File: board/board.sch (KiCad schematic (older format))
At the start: 15 parts, among them J1 MOTION DETECTOR, J2 EXT BUTTON, U3 ATTINY85-20PU

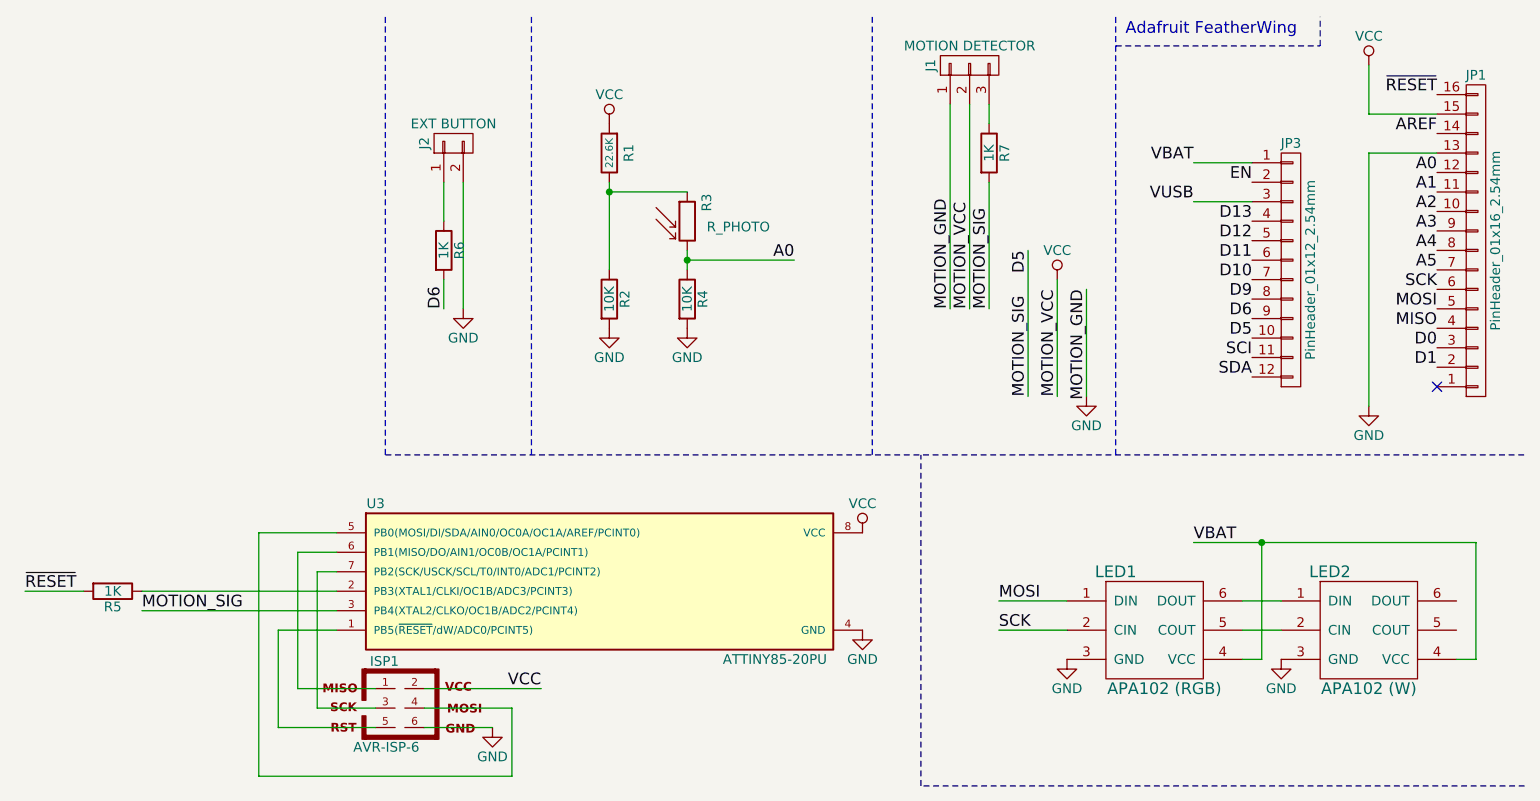
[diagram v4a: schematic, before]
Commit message: Fix photoresistor circuit
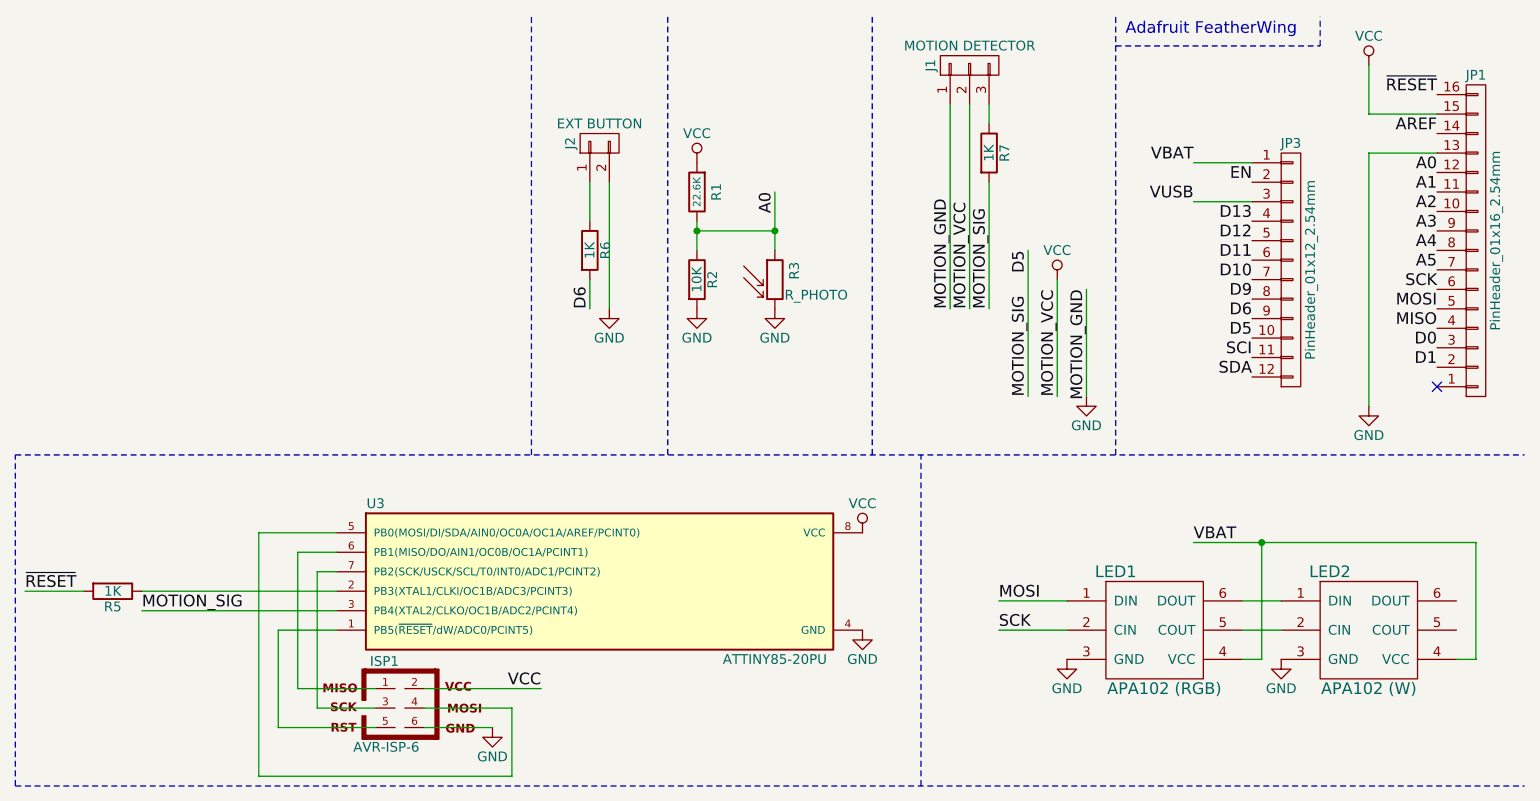
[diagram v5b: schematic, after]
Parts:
- removed R4: 10K, Resistors_SMD:R_0805_HandSoldering, symbol R
- J2: footprint Pin_Headers:Pin_Header_Angled_1x02_Pitch2.54mm -> Pin_Headers:Pin_Header_Straight_1x02_Pitch2.54mm
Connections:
- net A0: now also R1.1, R2.1, R3.1; no longer R3.2
- net GND: now also R3.2
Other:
- moved on the sheet: J2, R1, R2, R3, R6
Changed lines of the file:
@@
 SDA
 Wire Notes Line
-	4650 2750 10500 2750
+	2750 2750 10500 2750
 Wire Notes Line
 	8400 2750 8400 500
@@
 L R_PHOTO R3
 U 1 1 59797B58
-P 6200 1550
-F 0 "R3" V 6300 1600 50  0000 L CNN
-F 1 "R_PHOTO" H 6300 1550 50  0000 L TNN
-F 2 "Opto-Devices:Resistor_LDR_5.1x4.3_RM3.4" V 6250 1300 50  0001 L CNN
-F 3 "" H 6200 1500 50  0001 C CNN
-	1    6200 1550
+P 6650 1850
+F 0 "R3" V 6750 1850 50  0000 L CNN
+F 1 "R_PHOTO" H 6700 1800 50  0000 L TNN
+F 2 "Opto-Devices:Resistor_LDR_5.1x4.3_RM3.4" V 6700 1600 50  0001 L CNN
+F 3 "" H 6650 1800 50  0001 C CNN
+	1    6650 1850
 	1    0    0    -1
 $EndComp
@@
 L R R1
 U 1 1 597CE41F
-P 5800 1200
-F 0 "R1" V 5700 1200 50  0000 C CNN
-F 1 "22.6K" V 5800 1200 39  0000 C CNN
-F 2 "Resistors_SMD:R_0805_HandSoldering" V 5730 1200 50  0001 C CNN
-F 3 "" H 5800 1200 50  0001 C CNN
-	1    5800 1200
+P 6250 1400
+F 0 "R1" V 6150 1400 50  0000 C CNN
+F 1 "22.6K" V 6250 1400 39  0000 C CNN
+F 2 "Resistors_SMD:R_0805_HandSoldering" V 6180 1400 50  0001 C CNN
+F 3 "" H 6250 1400 50  0001 C CNN
+	1    6250 1400
 	-1   0    0    1
 $EndComp
@@
 L R R2
 U 1 1 597CE47C
-P 5800 1950
-F 0 "R2" V 5880 1950 50  0000 C CNN
-F 1 "10K" V 5800 1950 50  0000 C CNN
-F 2 "Resistors_SMD:R_0805_HandSoldering" V 5730 1950 50  0001 C CNN
-F 3 "" H 5800 1950 50  0001 C CNN
-	1    5800 1950
-	1    0    0    -1
-$EndComp
-Wire Wire Line
-	5800 1350 5800 1800
-Wire Wire Line
-	5800 1400 6200 1400
-Connection ~ 5800 1400
+P 6250 1850
+F 0 "R2" V 6330 1850 50  0000 C CNN
+F 1 "10K" V 6250 1850 50  0000 C CNN
+F 2 "Resistors_SMD:R_0805_HandSoldering" V 6180 1850 50  0001 C CNN
+F 3 "" H 6250 1850 50  0001 C CNN
+	1    6250 1850
+	1    0    0    -1
+$EndComp
+Wire Wire Line
+	6250 1550 6250 1700
+Connection ~ 6250 1600
 $Comp
 L GND #PWR04
 U 1 1 597CE63C
-P 5800 2100
-F 0 "#PWR04" H 5800 1850 50  0001 C CNN
-F 1 "GND" H 5800 1950 50  0000 C CNN
-F 2 "" H 5800 2100 50  0001 C CNN
-F 3 "" H 5800 2100 50  0001 C CNN
-	1    5800 2100
+P 6250 2000
+F 0 "#PWR04" H 6250 1750 50  0001 C CNN
+F 1 "GND" H 6250 1850 50  0000 C CNN
+F 2 "" H 6250 2000 50  0001 C CNN
+F 3 "" H 6250 2000 50  0001 C CNN
+	1    6250 2000
 	1    0    0    -1
 $EndComp
@@
 L VCC #PWR05
 U 1 1 597CEF49
-P 5800 1050
-F 0 "#PWR05" H 5800 900 50  0001 C CNN
-F 1 "VCC" H 5800 1200 50  0000 C CNN
-F 2 "" H 5800 1050 50  0001 C CNN
-F 3 "" H 5800 1050 50  0001 C CNN
-	1    5800 1050
-	1    0    0    -1
-$EndComp
-Text Label 6750 1750 2    60   ~ 0
+P 6250 1250
+F 0 "#PWR05" H 6250 1100 50  0001 C CNN
+F 1 "VCC" H 6250 1400 50  0000 C CNN
+F 2 "" H 6250 1250 50  0001 C CNN
+F 3 "" H 6250 1250 50  0001 C CNN
+	1    6250 1250
+	1    0    0    -1
+$EndComp
+Text Label 6650 1400 3    60   ~ 0
 A0
-Wire Wire Line
-	6200 1750 6750 1750
-$Comp
-L R R4
-U 1 1 597D09D1
-P 6200 1950
-F 0 "R4" V 6280 1950 50  0000 C CNN
-F 1 "10K" V 6200 1950 50  0000 C CNN
-F 2 "Resistors_SMD:R_0805_HandSoldering" V 6130 1950 50  0001 C CNN
-F 3 "" H 6200 1950 50  0001 C CNN
-	1    6200 1950
-	1    0    0    -1
-$EndComp
 $Comp
 L GND #PWR06
 U 1 1 597D0A0F
-P 6200 2100
-F 0 "#PWR06" H 6200 1850 50  0001 C CNN
-F 1 "GND" H 6200 1950 50  0000 C CNN
-F 2 "" H 6200 2100 50  0001 C CNN
-F 3 "" H 6200 2100 50  0001 C CNN
-	1    6200 2100
-	1    0    0    -1
-$EndComp
-Wire Wire Line
-	6200 1700 6200 1800
-Connection ~ 6200 1750
+P 6650 2000
+F 0 "#PWR06" H 6650 1750 50  0001 C CNN
+F 1 "GND" H 6650 1850 50  0000 C CNN
+F 2 "" H 6650 2000 50  0001 C CNN
+F 3 "" H 6650 2000 50  0001 C CNN
+	1    6650 2000
+	1    0    0    -1
+$EndComp
+Wire Wire Line
+	6650 1400 6650 1700
+Connection ~ 6650 1600
 $Comp
 L GND #PWR07
@@
 	7150 2750 7150 500
 Wire Notes Line
-	5400 2750 5400 500
-Wire Notes Line
-	10500 4450 7400 4450
+	6100 2750 6100 500
+Wire Notes Line
+	2750 4450 10500 4450
 Wire Notes Line
 	7400 4450 7400 2750
@@
 L CONN_01X02 J2
 U 1 1 597D1FB0
-P 5000 1150
-F 0 "J2" H 5000 1300 50  0000 C CNN
-F 1 "EXT BUTTON" V 5100 1150 50  0000 C CNN
-F 2 "Pin_Headers:Pin_Header_Angled_1x02_Pitch2.54mm" H 5000 1150 50  0001 C CNN
-F 3 "" H 5000 1150 50  0001 C CNN
-	1    5000 1150
+P 5750 1150
+F 0 "J2" H 5750 1300 50  0000 C CNN
+F 1 "EXT BUTTON" V 5850 1150 50  0000 C CNN
+F 2 "Pin_Headers:Pin_Header_Straight_1x02_Pitch2.54mm" H 5750 1150 50  0001 C CNN
+F 3 "" H 5750 1150 50  0001 C CNN
+	1    5750 1150
 	0    -1   -1   0
 $EndComp
@@
 L GND #PWR08
 U 1 1 597D2087
-P 5050 2000
-F 0 "#PWR08" H 5050 1750 50  0001 C CNN
-F 1 "GND" H 5050 1850 50  0000 C CNN
-F 2 "" H 5050 2000 50  0001 C CNN
-F 3 "" H 5050 2000 50  0001 C CNN
-	1    5050 2000
-	1    0    0    -1
-$EndComp
-Wire Wire Line
-	5050 1350 5050 2000
-Wire Wire Line
-	4950 1350 4950 1550
-Text Label 4950 2000 1    60   ~ 0
+P 5800 2000
+F 0 "#PWR08" H 5800 1750 50  0001 C CNN
+F 1 "GND" H 5800 1850 50  0000 C CNN
+F 2 "" H 5800 2000 50  0001 C CNN
+F 3 "" H 5800 2000 50  0001 C CNN
+	1    5800 2000
+	1    0    0    -1
+$EndComp
+Wire Wire Line
+	5800 1350 5800 2000
+Wire Wire Line
+	5700 1350 5700 1550
+Text Label 5700 2000 1    60   ~ 0
 D6
 Wire Notes Line
-	4650 2750 4650 500
+	5400 2750 5400 500
 $Comp
 L ATTINY85-20PU U3
@@
 L R R6
 U 1 1 5982A5C8
-P 4950 1700
-F 0 "R6" V 5030 1700 50  0000 C CNN
-F 1 "1K" V 4950 1700 50  0000 C CNN
-F 2 "Resistors_SMD:R_0805_HandSoldering" V 4880 1700 50  0001 C CNN
-F 3 "" H 4950 1700 50  0001 C CNN
-	1    4950 1700
-	1    0    0    -1
-$EndComp
-Wire Wire Line
-	4950 1850 4950 2000
+P 5700 1700
+F 0 "R6" V 5780 1700 50  0000 C CNN
+F 1 "1K" V 5700 1700 50  0000 C CNN
+F 2 "Resistors_SMD:R_0805_HandSoldering" V 5630 1700 50  0001 C CNN
+F 3 "" H 5700 1700 50  0001 C CNN
+	1    5700 1700
+	1    0    0    -1
+$EndComp
+Wire Wire Line
+	5700 1850 5700 2000
 $Comp
 L R R7
@@
 $EndComp
 $Comp
-L VCC #PWR?
+L VCC #PWR013
 U 1 1 5987EE9E
 P 7100 3150
-F 0 "#PWR?" H 7100 3000 50  0001 C CNN
+F 0 "#PWR013" H 7100 3000 50  0001 C CNN
 F 1 "VCC" H 7100 3300 50  0000 C CNN
 F 2 "" H 7100 3150 50  0001 C CNN
@@
 	1    0    0    -1
 $EndComp
+Wire Wire Line
+	6250 1600 6650 1600
+Wire Notes Line
+	2750 4450 2750 2750
 $EndSCHEMATC

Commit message: Add I2C lines between between attiny and ESP8266
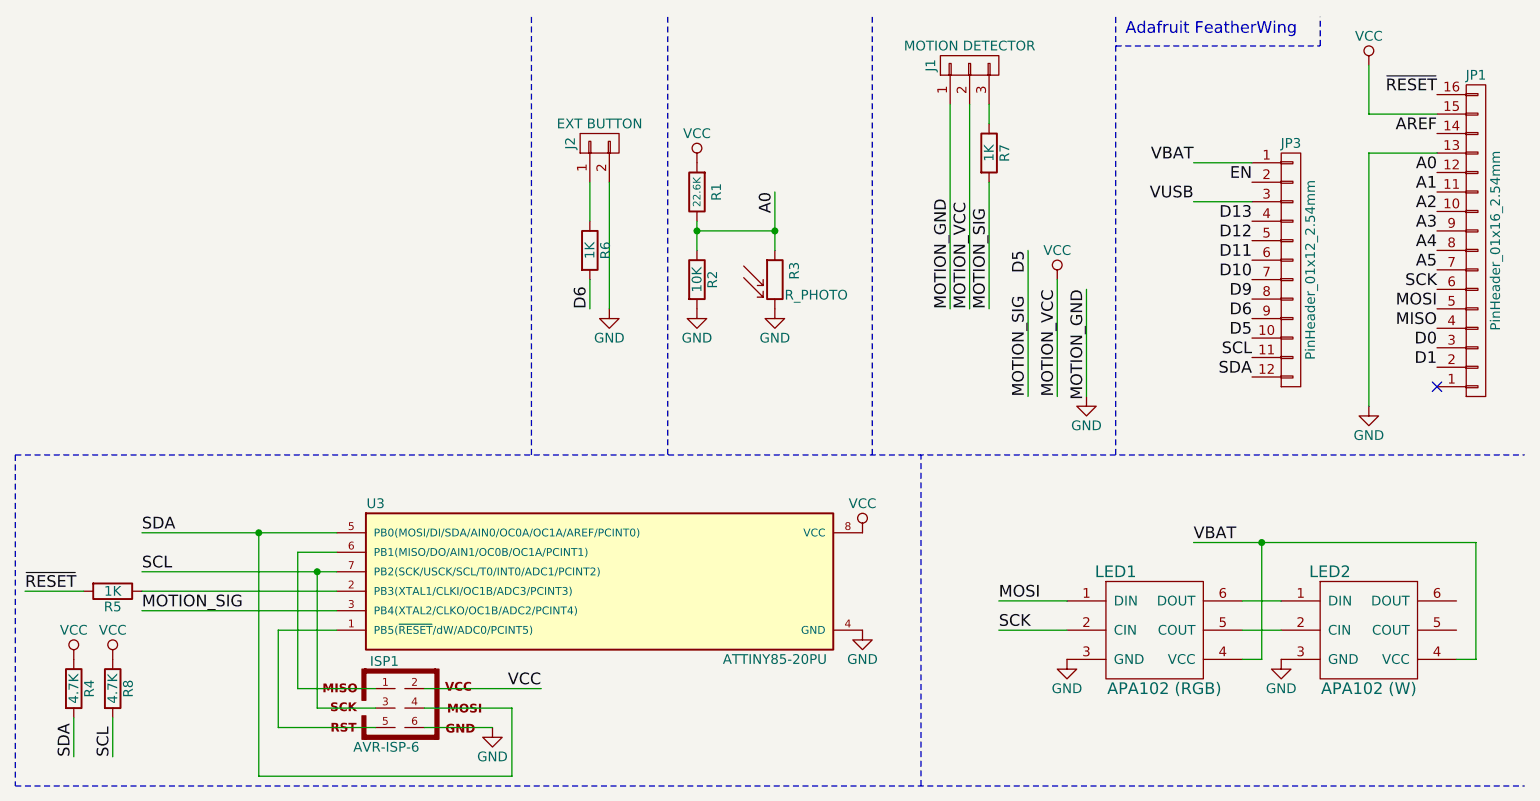
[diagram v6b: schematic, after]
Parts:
- added R4, R8: 4.7K, symbol R
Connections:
- net SCI is gone; now on net SCL: JP3.11 (P11)
- net SDA: now also ISP1.4, U3.5 (PB0(MOSI/DI/SDA/AIN0/OC0A/OC1A/AREF/PCINT0)), R4.2
- net VCC: now also R4.1, R8.1
- net SCL: now reaches ISP1.3, U3.7 (PB2(SCK/USCK/SCL/T0/INT0/ADC1/PCINT2))
- net SCL: now also R8.2
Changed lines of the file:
@@
 Adafruit FeatherWing\n
 $Comp
-L VCC #PWR01
+L VCC #PWR14
 U 1 1 56D753B8
 P 9700 750
-F 0 "#PWR01" H 9700 600 50  0001 C CNN
+F 0 "#PWR14" H 9700 600 50  0001 C CNN
 F 1 "VCC" H 9700 900 50  0000 C CNN
 F 2 "" H 9700 750 50  0000 C CNN
@@
 $EndComp
 $Comp
-L GND #PWR02
+L GND #PWR15
 U 1 1 56D75A03
 P 9700 2500
-F 0 "#PWR02" H 9700 2250 50  0001 C CNN
+F 0 "#PWR15" H 9700 2250 50  0001 C CNN
 F 1 "GND" H 9700 2350 50  0000 C CNN
 F 2 "" H 9700 2500 50  0000 C CNN
@@
 D5
 Text Label 9100 2250 2    60   ~ 0
-SCI
+SCL
 Text Label 9100 2350 2    60   ~ 0
 SDA
@@
 NoConn ~ 10050 2400
 $Comp
-L GND #PWR03
+L GND #PWR11
 U 1 1 59796D2F
 P 8150 3800
-F 0 "#PWR03" H 8150 3550 50  0001 C CNN
+F 0 "#PWR11" H 8150 3550 50  0001 C CNN
 F 1 "GND" H 8150 3650 50  0000 C CNN
 F 2 "" H 8150 3800 50  0001 C CNN
@@
 Connection ~ 6250 1600
 $Comp
-L GND #PWR04
+L GND #PWR6
 U 1 1 597CE63C
 P 6250 2000
-F 0 "#PWR04" H 6250 1750 50  0001 C CNN
+F 0 "#PWR6" H 6250 1750 50  0001 C CNN
 F 1 "GND" H 6250 1850 50  0000 C CNN
 F 2 "" H 6250 2000 50  0001 C CNN
@@
 $EndComp
 $Comp
-L VCC #PWR05
+L VCC #PWR5
 U 1 1 597CEF49
 P 6250 1250
-F 0 "#PWR05" H 6250 1100 50  0001 C CNN
+F 0 "#PWR5" H 6250 1100 50  0001 C CNN
 F 1 "VCC" H 6250 1400 50  0000 C CNN
 F 2 "" H 6250 1250 50  0001 C CNN
@@
 A0
 $Comp
-L GND #PWR06
+L GND #PWR7
 U 1 1 597D0A0F
 P 6650 2000
-F 0 "#PWR06" H 6650 1750 50  0001 C CNN
+F 0 "#PWR7" H 6650 1750 50  0001 C CNN
 F 1 "GND" H 6650 1850 50  0000 C CNN
 F 2 "" H 6650 2000 50  0001 C CNN
@@
 Connection ~ 6650 1600
 $Comp
-L GND #PWR07
+L GND #PWR12
 U 1 1 597D0EF3
 P 8250 2450
-F 0 "#PWR07" H 8250 2200 50  0001 C CNN
+F 0 "#PWR12" H 8250 2200 50  0001 C CNN
 F 1 "GND" H 8250 2300 50  0000 C CNN
 F 2 "" H 8250 2450 50  0001 C CNN
@@
 $EndComp
 $Comp
-L GND #PWR08
+L GND #PWR4
 U 1 1 597D2087
 P 5800 2000
-F 0 "#PWR08" H 5800 1750 50  0001 C CNN
+F 0 "#PWR4" H 5800 1750 50  0001 C CNN
 F 1 "GND" H 5800 1850 50  0000 C CNN
 F 2 "" H 5800 2000 50  0001 C CNN
@@
 $EndComp
 $Comp
-L GND #PWR09
+L GND #PWR9
 U 1 1 597D1088
 P 7100 3650
-F 0 "#PWR09" H 7100 3400 50  0001 C CNN
+F 0 "#PWR9" H 7100 3400 50  0001 C CNN
 F 1 "GND" H 7100 3500 50  0000 C CNN
 F 2 "" H 7100 3650 50  0001 C CNN
@@
 	4300 4050 4300 3350
 Wire Wire Line
-	4300 3350 4400 3350
-$Comp
-L GND #PWR010
+	3400 3350 4400 3350
+$Comp
+L GND #PWR3
 U 1 1 597D12FA
 P 5200 4150
-F 0 "#PWR010" H 5200 3900 50  0001 C CNN
+F 0 "#PWR3" H 5200 3900 50  0001 C CNN
 F 1 "GND" H 5200 4000 50  0000 C CNN
 F 2 "" H 5200 4150 50  0001 C CNN
@@
 	4000 3150 4000 4400
 Wire Wire Line
-	4000 3150 4400 3150
+	3400 3150 4400 3150
 Wire Wire Line
 	4850 4050 5300 4050
@@
 	8100 2450 8100 1850
 $Comp
-L VCC #PWR011
+L VCC #PWR10
 U 1 1 597D3E37
 P 8100 1850
-F 0 "#PWR011" H 8100 1700 50  0001 C CNN
+F 0 "#PWR10" H 8100 1700 50  0001 C CNN
 F 1 "VCC" H 8100 2000 50  0000 C CNN
 F 2 "" H 8100 1850 50  0001 C CNN
@@
 	7750 2000 7750 1350
 $Comp
-L GND #PWR012
+L GND #PWR13
 U 1 1 5986A206
 P 9250 3800
-F 0 "#PWR012" H 9250 3550 50  0001 C CNN
+F 0 "#PWR13" H 9250 3550 50  0001 C CNN
 F 1 "GND" H 9250 3650 50  0000 C CNN
 F 2 "" H 9250 3800 50  0001 C CNN
@@
 $EndComp
 $Comp
-L VCC #PWR013
+L VCC #PWR8
 U 1 1 5987EE9E
 P 7100 3150
-F 0 "#PWR013" H 7100 3000 50  0001 C CNN
+F 0 "#PWR8" H 7100 3000 50  0001 C CNN
 F 1 "VCC" H 7100 3300 50  0000 C CNN
 F 2 "" H 7100 3150 50  0001 C CNN
@@
 Wire Wire Line
 	6250 1600 6650 1600
-Wire Notes Line
-	2750 4450 2750 2750
+Connection ~ 4000 3150
+Connection ~ 4300 3350
+Text Label 3400 3350 0    60   ~ 0
+SCL
+Text Label 3400 3150 0    60   ~ 0
+SDA
+$Comp
+L VCC #PWR2
+U 1 1 598F5087
+P 3250 3800
+F 0 "#PWR2" H 3250 3650 50  0001 C CNN
+F 1 "VCC" H 3250 3950 50  0000 C CNN
+F 2 "" H 3250 3800 50  0001 C CNN
+F 3 "" H 3250 3800 50  0001 C CNN
+	1    3250 3800
+	1    0    0    -1
+$EndComp
+Wire Wire Line
+	3250 4100 3250 4300
+Text Label 3250 4300 1    60   ~ 0
+SCL
+$Comp
+L VCC #PWR1
+U 1 1 598F54B3
+P 3050 3800
+F 0 "#PWR1" H 3050 3650 50  0001 C CNN
+F 1 "VCC" H 3050 3950 50  0000 C CNN
+F 2 "" H 3050 3800 50  0001 C CNN
+F 3 "" H 3050 3800 50  0001 C CNN
+	1    3050 3800
+	1    0    0    -1
+$EndComp
+Wire Wire Line
+	3050 4100 3050 4300
+Text Label 3050 4300 1    60   ~ 0
+SDA
+Wire Notes Line
+	2750 2750 2750 4450
+$Comp
+L R R4
+U 1 1 598F56B4
+P 3050 3950
+F 0 "R4" V 3130 3950 50  0000 C CNN
+F 1 "4.7K" V 3050 3950 50  0000 C CNN
+F 2 "" V 2980 3950 50  0001 C CNN
+F 3 "" H 3050 3950 50  0001 C CNN
+	1    3050 3950
+	1    0    0    -1
+$EndComp
+$Comp
+L R R8
+U 1 1 598F56F9
+P 3250 3950
+F 0 "R8" V 3330 3950 50  0000 C CNN
+F 1 "4.7K" V 3250 3950 50  0000 C CNN
+F 2 "" V 3180 3950 50  0001 C CNN
+F 3 "" H 3250 3950 50  0001 C CNN
+	1    3250 3950
+	1    0    0    -1
+$EndComp
 $EndSCHEMATC
